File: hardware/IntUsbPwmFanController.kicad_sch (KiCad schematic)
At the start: 51 parts, among them J1 UsbPortA, J2 UsbPortB, J3 MOLEX, J4 VselA, J5 VselB, J6 FAN, J7 USB_Out, J8 GPIO, Q1 IRLML6402, U1 FT260S, U3 ATtiny202-SS

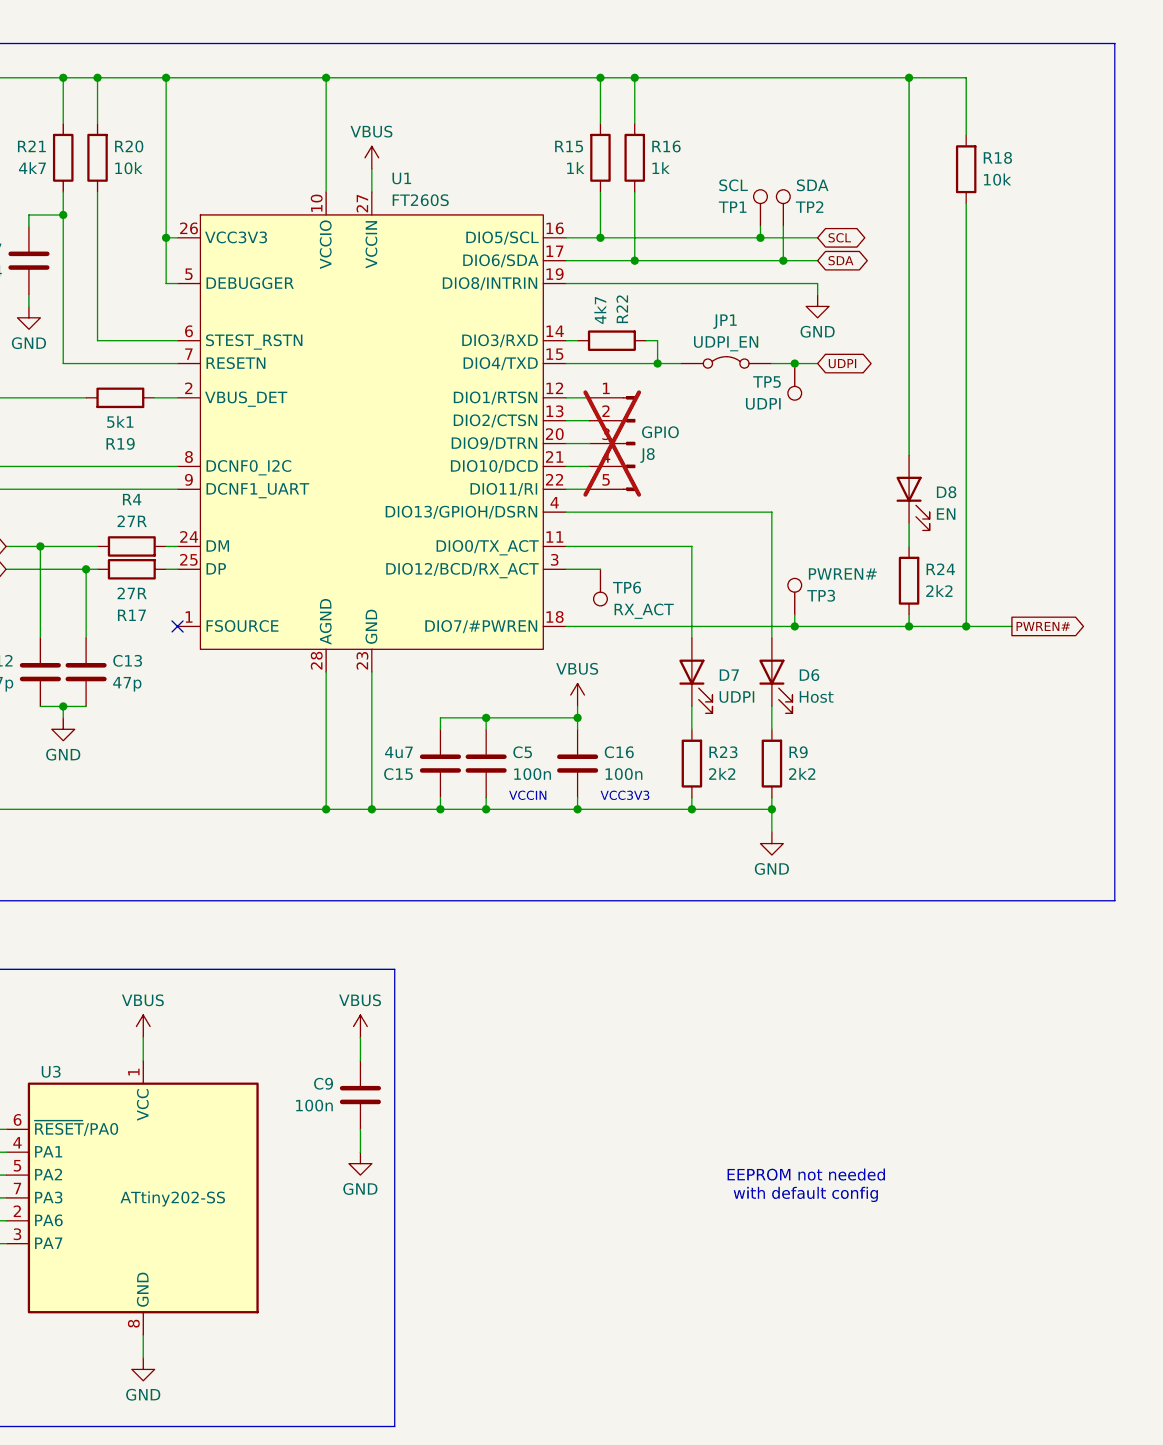
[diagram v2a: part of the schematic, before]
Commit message: Add (optional) configuration EEPROM
Since it has a very small footprint and optinal GPIO headers are also
available, add a configuration EEPROM to the design.
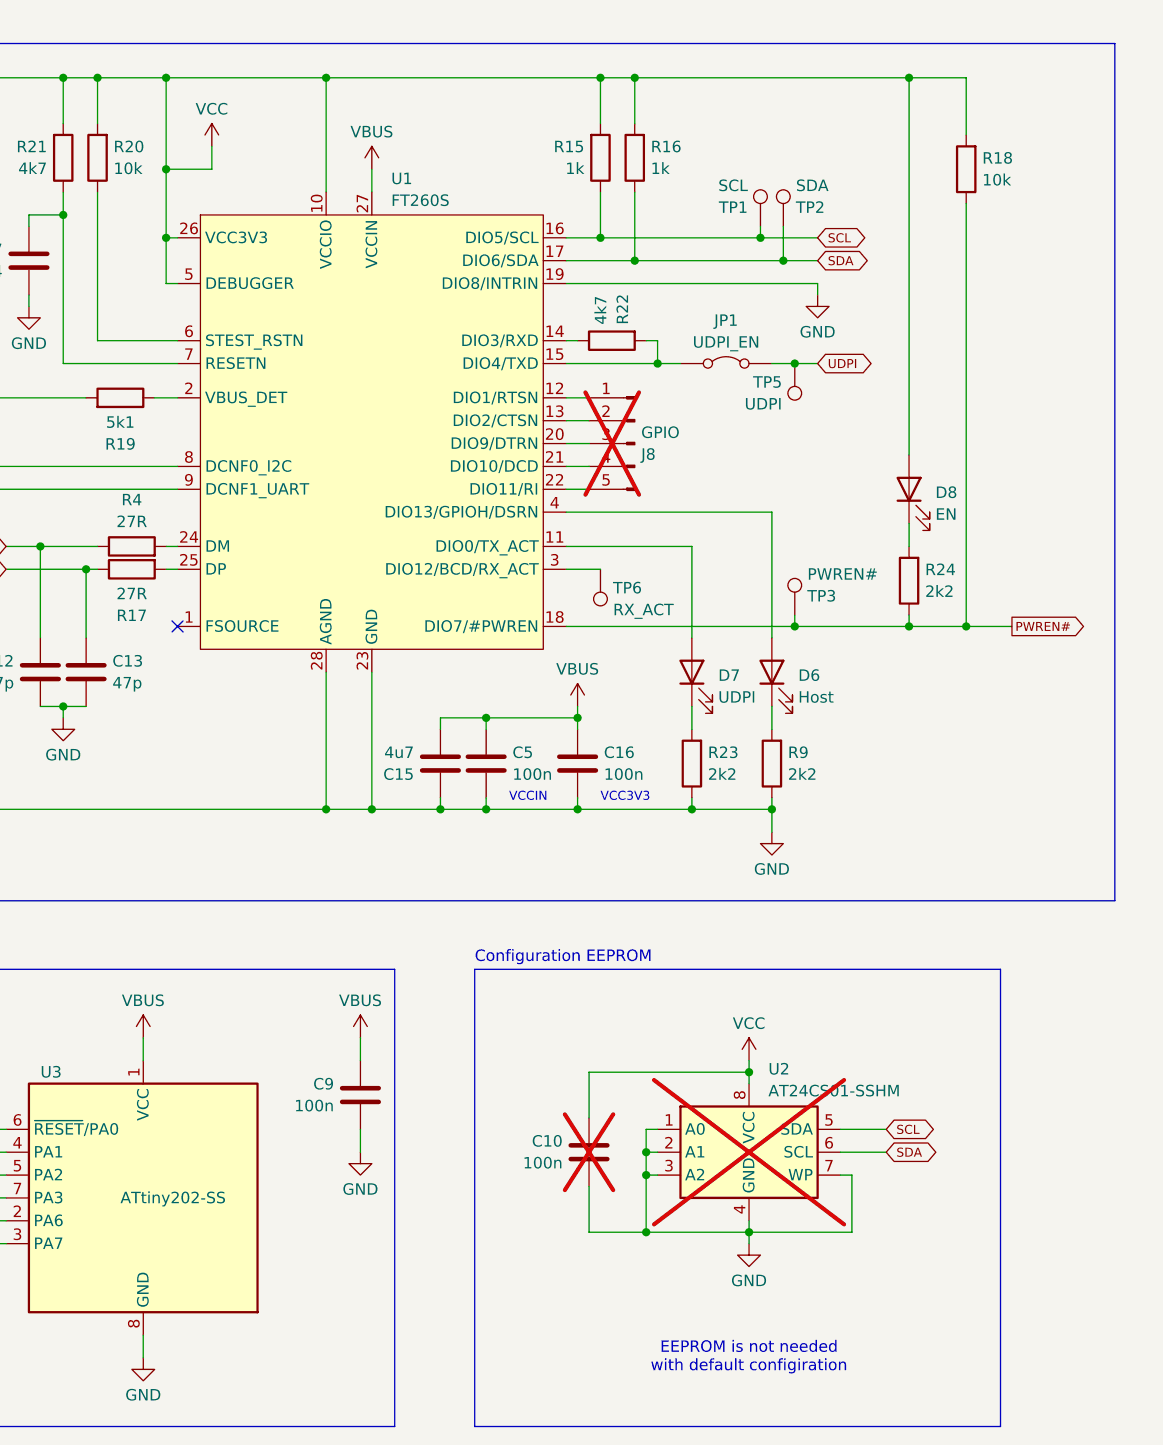
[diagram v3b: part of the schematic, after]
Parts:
- added C10: 100n, Capacitor_SMD:C_0603_1608Metric_Pad1.08x0.95mm_HandSolder, symbol Device:C
- added U2: AT24CS01-SSHM, Package_SO:SOIC-8_3.9x4.9mm_P1.27mm, symbol Memory_EEPROM:AT24CS01-SSHM
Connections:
- net GND: now also C10.2, U2.1 (A0), U2.2 (A1), U2.3 (A2), U2.4 (GND), U2.7 (WP)
- net SCL: now also U2.5 (SDA)
- net SDA: now also U2.6 (SCL)
- net VCC: now reaches D8.2 (A), JP3.1 (A), R15.2, R16.2, R18.2, R20.2, R21.2, U1.10 (VCCIO), U1.26 (VCC3V3), U1.5 (DEBUGGER), U1.8 (DCNF0_I2C)
- net VCC: now also C10.1, U2.8 (VCC)
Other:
- note added: "Configuration EEPROM"
- note added: "EEPROM is not needed with default configiration"
- note removed: "EEPROM not needed with default config"

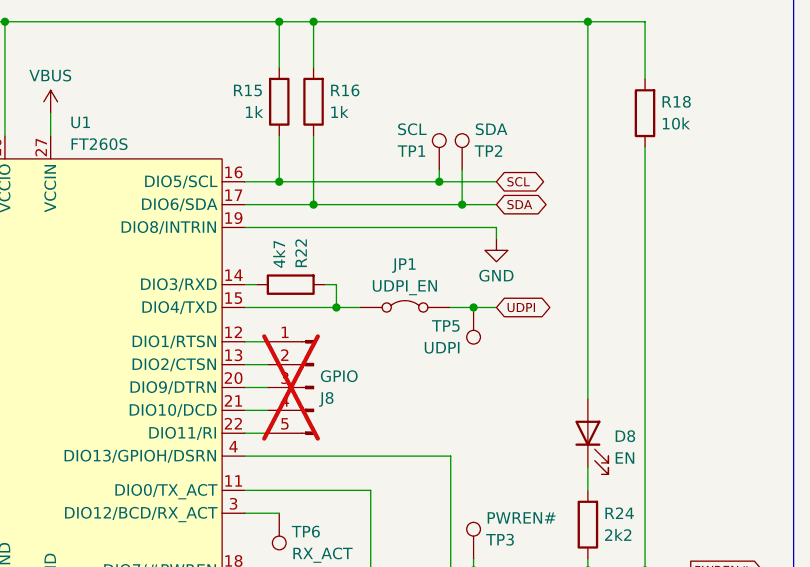
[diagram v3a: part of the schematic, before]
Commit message: Fix the solder jumpers
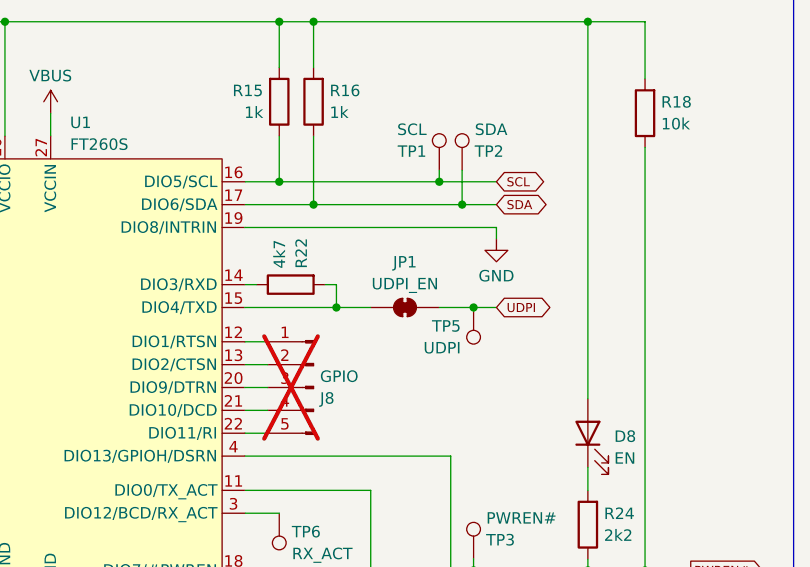
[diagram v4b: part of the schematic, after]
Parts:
- JP1: symbol Jumper:Jumper_2_Bridged -> Jumper:SolderJumper_2_Bridged; now left out of the parts list
- JP3: footprint (none) -> Jumper:SolderJumper-3_P1.3mm_Bridged12_RoundedPad1.0x1.5mm
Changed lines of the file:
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@@
 	(wire
 		(pts
-			(xy 110.49 53.34) (xy 113.03 53.34)
+			(xy 110.49 53.34) (xy 114.3 53.34)
 		)
 		(stroke
@@
 	(wire
 		(pts
+			(xy 121.92 53.34) (xy 125.73 53.34)
+		)
+		(stroke
+			(width 0)
+			(type default)
+		)
+	)
+	(wire
+		(pts
 			(xy 48.26 50.8) (xy 48.26 34.29)
 		)
@@
 	(wire
 		(pts
-			(xy 123.19 53.34) (xy 125.73 53.34)
-		)
-		(stroke
-			(width 0)
-			(type default)
-		)
-	)
-	(wire
-		(pts
 			(xy 199.39 144.145) (xy 199.39 139.065)
 		)
@@
 			)
 		)
-		(property "Footprint" ""
+		(property "Footprint" "Jumper:SolderJumper-3_P1.3mm_Bridged12_RoundedPad1.0x1.5mm"
 			(at 20.32 67.31 0)
 			(effects
@@
 	)
 	(symbol
-		(lib_id "Jumper:Jumper_2_Bridged")
+		(lib_id "Jumper:SolderJumper_2_Bridged")
 		(at 118.11 53.34 0)
 		(unit 1)
 		(exclude_from_sim no)
-		(in_bom yes)
+		(in_bom no)
 		(on_board yes)
 		(dnp no)
 		(fields_autoplaced yes)
 		(property "Reference" "JP1"
-			(at 118.11 48.5605 0)
+			(at 118.11 48.3065 0)
 			(effects
 				(font
@@
 		)
 		(property "Value" "UDPI_EN"
-			(at 118.11 50.9848 0)
+			(at 118.11 50.7308 0)
 			(effects
 				(font
@@
 			)
 		)
-		(property "Description" "Jumper, 2-pole, closed/bridged"
+		(property "Description" "Solder Jumper, 2-pole, closed/bridged"
 			(at 118.11 53.34 0)
 			(effects

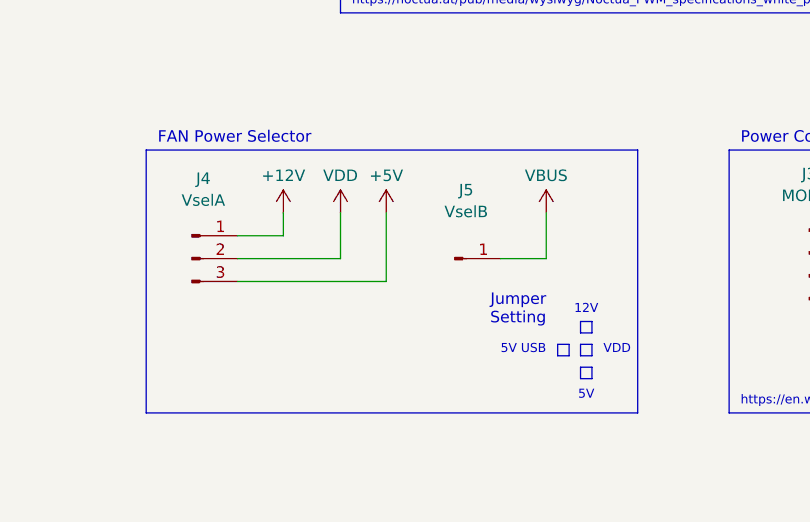
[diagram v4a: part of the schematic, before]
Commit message: Use new symbol for the 3-way jumper
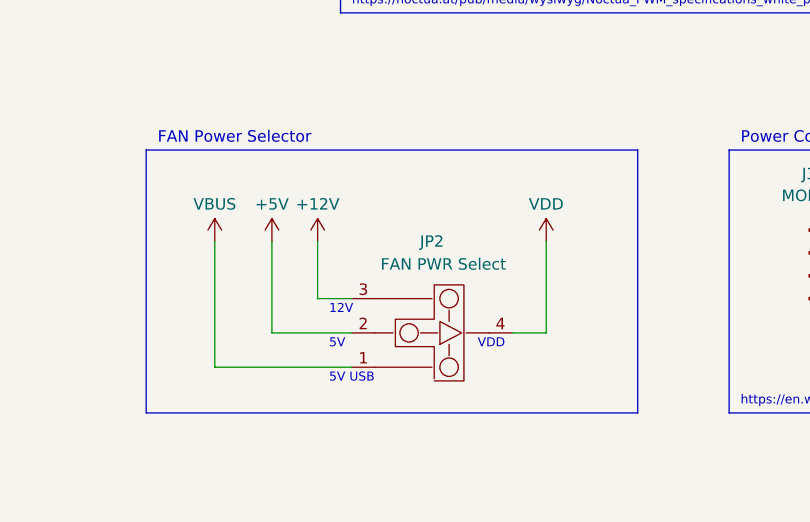
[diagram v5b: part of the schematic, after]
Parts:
- removed J4: VselA, Connector_PinSocket_2.54mm:PinSocket_1x03_P2.54mm_Vertical, symbol Connector:Conn_01x03_Pin
- removed J5: VselB, Connector_PinSocket_2.54mm:PinSocket_1x01_P2.54mm_Vertical, symbol Connector:Conn_01x01_Pin
- added JP2: FAN PWR Select, ThreeWayJumper:ThreeWayJumper, symbol ThreeWayJumper:ThreeWayJumper
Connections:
- net +12V: now also JP2.3 (OPT3)
- net +5V: now also JP2.2 (OPT2)
- net VBUS: now also JP2.1 (OPT1)
- net VDD: now also JP2.4 (SEL)
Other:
- note removed: "Jumper Setting"

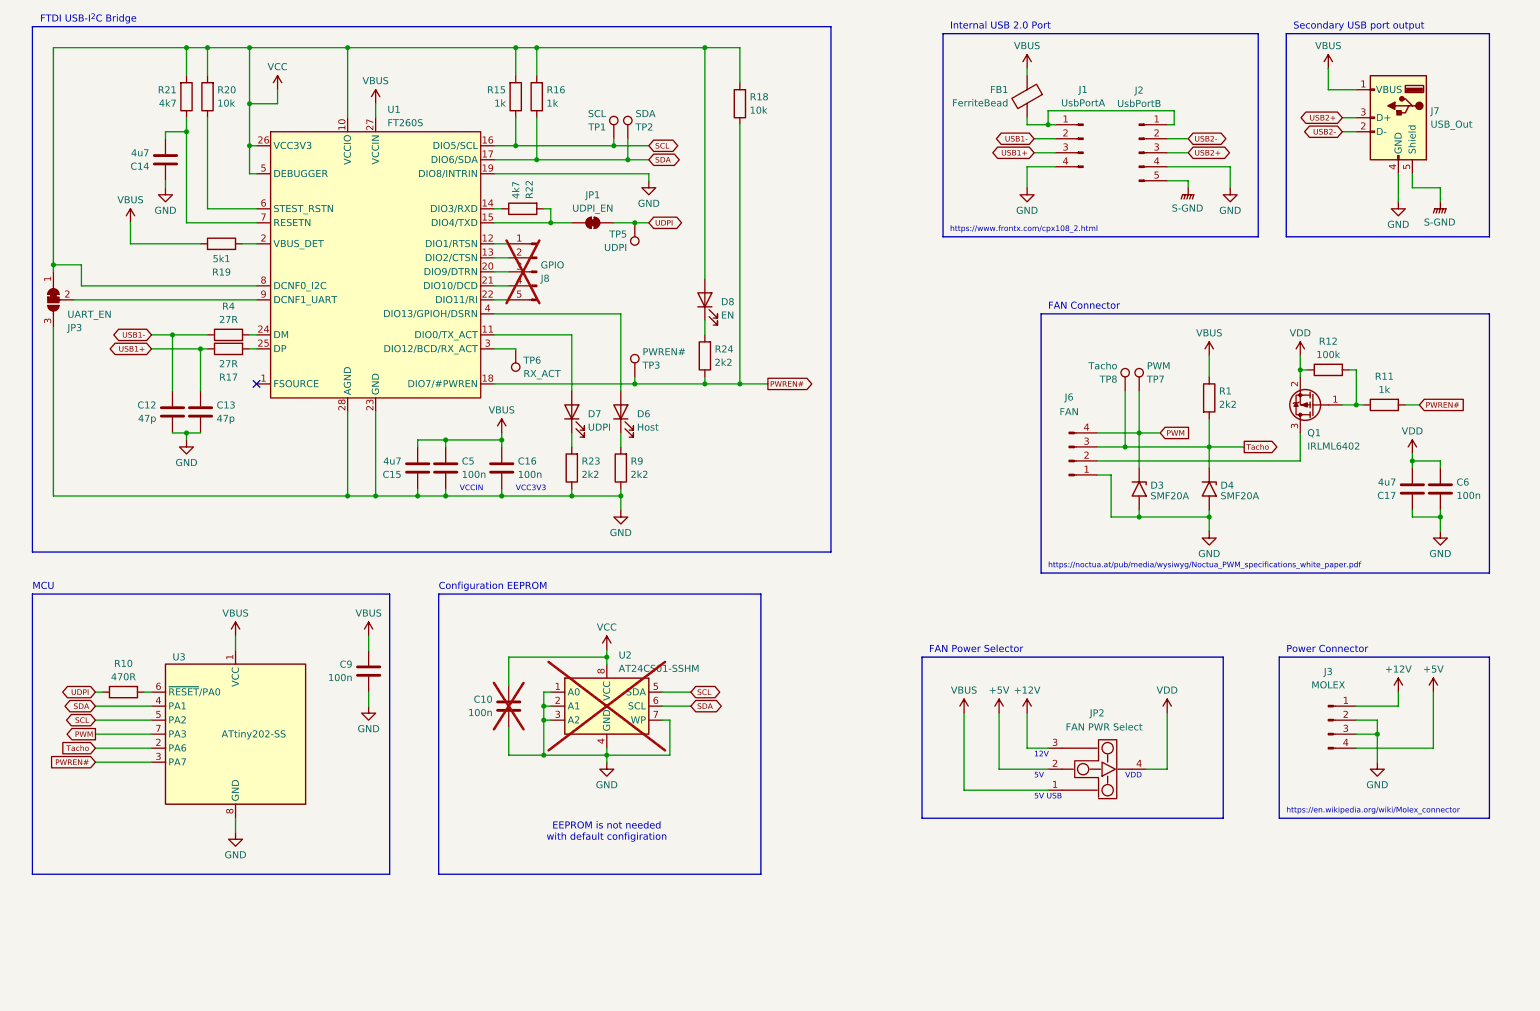
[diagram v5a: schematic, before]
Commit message: Improve fan connector filtering
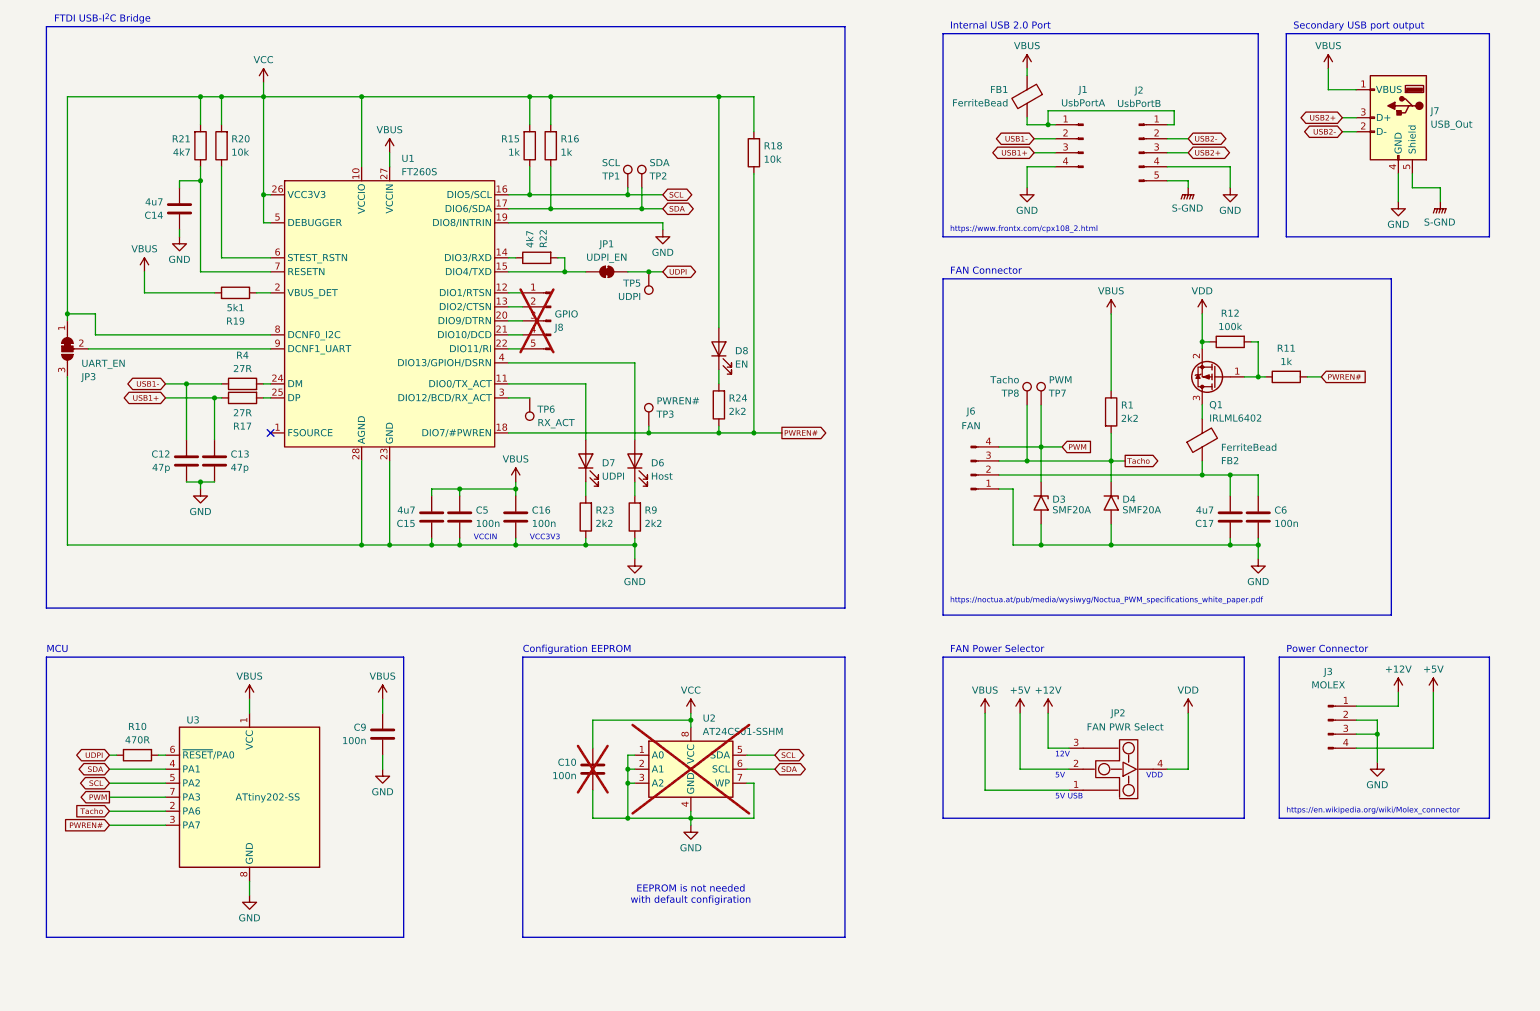
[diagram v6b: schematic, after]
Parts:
- added FB2: FerriteBead, Resistor_SMD:R_0603_1608Metric_Pad0.98x0.95mm_HandSolder, symbol Device:FerriteBead
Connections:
- net VDD: no longer C17.2, C6.1
- net at J6.2 (Pin_2): now also C17.2, C6.1, FB2.1; no longer Q1.3 (D)
- new net: FB2.2, Q1.3 (D)
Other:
- moved on the sheet: C10, C12, C13, C14, C15, C16, C17, C5, C6, C9, D3, D4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
